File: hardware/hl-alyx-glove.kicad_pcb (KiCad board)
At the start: 2 copper layers, 2 parts, among them U1 MAX7219

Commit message: schematic first version
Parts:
- added D1: GREEN, LED_THT:LED_D5.0mm, F.Cu at (100.0, 49.0)
- added D2: GREEN, LED_THT:LED_D5.0mm, F.Cu at (95.0, 49.0)
- added D3: RED, LED_SMD:LED_2010_5025Metric, F.Cu at (169.0, 61.0)
- added J1: OLED, Connector_PinSocket_2.54mm:PinSocket_1x04_P2.54mm_Horizontal, B.Cu at (155.0, 97.0)
- added LED2: 788BS, CustomComponents:788BS, F.Cu at (123.5, 74.2)
- added LED3: 788BS, CustomComponents:788BS, F.Cu at (146.8, 74.6)
- added R1: 10K, Resistor_THT:R_Axial_DIN0309_L9.0mm_D3.2mm_P12.70mm_Horizontal, F.Cu at (106.0, 88.0)
- added R2: 10K, Resistor_THT:R_Axial_DIN0309_L9.0mm_D3.2mm_P12.70mm_Horizontal, F.Cu at (129.0, 88.0)
- added R3: 10K, Resistor_THT:R_Axial_DIN0309_L9.0mm_D3.2mm_P12.70mm_Horizontal, F.Cu at (152.0, 88.0)
- added R4: 10K, Resistor_THT:R_Axial_DIN0309_L9.0mm_D3.2mm_P12.70mm_Horizontal, F.Cu at (137.0, 49.0)
- added R5: 68, Resistor_THT:R_Axial_DIN0309_L9.0mm_D3.2mm_P12.70mm_Horizontal, F.Cu at (107.0, 57.0)
- added R6: 68, Resistor_THT:R_Axial_DIN0309_L9.0mm_D3.2mm_P12.70mm_Horizontal, F.Cu at (91.0, 60.0)
- added R7: 100, Resistor_THT:R_Axial_DIN0309_L9.0mm_D3.2mm_P12.70mm_Horizontal, F.Cu at (167.0, 49.0)
- added U2: MAX7219, Package_SO:SOP-24_7.5x15.4mm_P1.27mm, B.Cu at (123.5, 74.9)
- added U3: MAX7219, Package_SO:SOP-24_7.5x15.4mm_P1.27mm, B.Cu at (147.0, 74.6)
- added U4: ATmega328P-PU, Package_DIP:DIP-28_W7.62mm, F.Cu at (156.0, 53.0)
- U1: moved to B.Cu
- moved LED1 44.8 mm to (100.5, 73.8)
- moved U1 44.7 mm to (100.5, 73.8)
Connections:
- net Net-(U1-Pad4) renamed GND
- LED1 pad 1: Net-(LED1-Pad1) -> /LED_Matrix_0/C4
- LED1 pad 10: Net-(LED1-Pad10) -> /LED_Matrix_0/R4
- LED1 pad 11: Net-(LED1-Pad11) -> /LED_Matrix_0/R6
- LED1 pad 12: Net-(LED1-Pad12) -> /LED_Matrix_0/C5
- LED1 pad 13: Net-(LED1-Pad13) -> /LED_Matrix_0/R1
- LED1 pad 14: Net-(LED1-Pad14) -> /LED_Matrix_0/C7
- LED1 pad 15: Net-(LED1-Pad15) -> /LED_Matrix_0/R7
- LED1 pad 16: Net-(LED1-Pad16) -> /LED_Matrix_0/R8
- LED1 pad 2: Net-(LED1-Pad2) -> /LED_Matrix_0/C2
- LED1 pad 3: Net-(LED1-Pad3) -> /LED_Matrix_0/R2
- LED1 pad 4: Net-(LED1-Pad4) -> /LED_Matrix_0/R3
- LED1 pad 5: Net-(LED1-Pad5) -> /LED_Matrix_0/C1
- LED1 pad 6: Net-(LED1-Pad6) -> /LED_Matrix_0/R5
- LED1 pad 7: Net-(LED1-Pad7) -> /LED_Matrix_0/C3
- LED1 pad 8: Net-(LED1-Pad8) -> /LED_Matrix_0/C6
- LED1 pad 9: Net-(LED1-Pad9) -> /LED_Matrix_0/C8
- U1 pad 1: Net-(U1-Pad1) -> /LED_Matrix_0/DIN
- U1 pad 10: Net-(U1-Pad10) -> /LED_Matrix_0/R6
- U1 pad 11: Net-(U1-Pad11) -> /LED_Matrix_0/R2
- U1 pad 12: Net-(U1-Pad12) -> /LED_Matrix_0/LOAD
- U1 pad 13: Net-(U1-Pad13) -> /LED_Matrix_0/CLK
- U1 pad 14: Net-(U1-Pad14) -> /LED_Matrix_0/C2
- U1 pad 15: Net-(U1-Pad15) -> /LED_Matrix_0/C7
- U1 pad 16: Net-(U1-Pad16) -> /LED_Matrix_0/C3
- U1 pad 17: Net-(U1-Pad17) -> /LED_Matrix_0/C8
- U1 pad 2: Net-(U1-Pad2) -> /LED_Matrix_0/R1
- U1 pad 20: Net-(U1-Pad20) -> /LED_Matrix_0/C4
- U1 pad 21: Net-(LED1-Pad2) -> /LED_Matrix_0/C6
- U1 pad 22: Net-(U1-Pad22) -> /LED_Matrix_0/C1
- U1 pad 23: Net-(U1-Pad23) -> /LED_Matrix_0/C5
- U1 pad 24: Net-(U1-Pad24) -> /LED_Matrix_1/DIN
- U1 pad 3: Net-(U1-Pad3) -> /LED_Matrix_0/R5
- U1 pad 5: Net-(U1-Pad5) -> /LED_Matrix_0/R7
- U1 pad 6: Net-(U1-Pad6) -> /LED_Matrix_0/R3
- U1 pad 7: Net-(U1-Pad7) -> /LED_Matrix_0/R4
- U1 pad 8: Net-(U1-Pad8) -> /LED_Matrix_0/R8
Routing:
- net /LED_Matrix_1/R7: track 0.00 -> 26.6 mm, vias 0 -> 3
- net /LED_Matrix_2/R6: track 0.00 -> 22.5 mm, vias 0 -> 1
- net /LED_Matrix_1/R6: track 0.00 -> 22.5 mm, vias 0 -> 1
- net /LED_Matrix_0/R6: track 0.00 -> 22.5 mm, vias 0 -> 1
- net GND: track 0.00 -> 21.0 mm, vias 0 -> 4
- net /LED_Matrix_2/C3: track 0.00 -> 19.2 mm, vias 0 -> 3
- net /LED_Matrix_1/C3: track 0.00 -> 19.2 mm, vias 0 -> 3
- net /LED_Matrix_0/C3: track 0.00 -> 19.2 mm, vias 0 -> 3
- net /LED_Matrix_2/C4: track 0.00 -> 18.7 mm
- net /LED_Matrix_1/C4: track 0.00 -> 18.7 mm
- net /LED_Matrix_0/C4: track 0.00 -> 18.7 mm
- net /LED_Matrix_1/R4: track 0.00 -> 17.9 mm, vias 0 -> 1
- net /LED_Matrix_0/R4: track 0.00 -> 17.9 mm, vias 0 -> 1
- net /LED_Matrix_2/R4: track 0.00 -> 17.9 mm, vias 0 -> 1
- net /LED_Matrix_2/R1: track 0.00 -> 16.7 mm, vias 0 -> 1
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
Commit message: add some missing components
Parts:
- added C1: 100N, Capacitor_THT:C_Disc_D6.0mm_W2.5mm_P5.00mm, F.Cu at (126.0, 49.0)
- added J2: POWER, Connector_PinHeader_2.54mm:PinHeader_1x02_P2.54mm_Horizontal, F.Cu at (112.0, 44.0)
- moved U2 0.69 mm to (123.5, 74.2)
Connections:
- U1 pad 19: Net-(U1-Pad19) -> +3V3
- U2 pad 19: Net-(U2-Pad19) -> +3V3
- U3 pad 19: Net-(U3-Pad19) -> +3V3
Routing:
- net GND: track 21.0 -> 31.6 mm, vias 4 -> 6
- net /LED_Matrix_1/R7: track 26.6 -> 16.1 mm, vias 3 -> 1

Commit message: pcb first version
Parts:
- added REF**: MountingHole_3.2mm_M3, MountingHole:MountingHole_3.2mm_M3, F.Cu at (88.0, 90.0)
- added REF**: MountingHole_3.2mm_M3, MountingHole:MountingHole_3.2mm_M3, F.Cu at (88.0, 54.0)
- added REF**: MountingHole_3.2mm_M3, MountingHole:MountingHole_3.2mm_M3, F.Cu at (170.0, 48.0)
- added REF**: MountingHole_3.2mm_M3, MountingHole:MountingHole_3.2mm_M3, F.Cu at (145.0, 90.0)
- D3: footprint LED_SMD:LED_2010_5025Metric -> LED_SMD:LED_RGB_5050-6
- J2: moved to B.Cu
- R7: value 100 -> 180
- moved J2 36.8 mm to (87.0, 71.0), turned to 180 degrees
- moved R4 34.1 mm to (171.0, 51.5), turned to 180 degrees
- moved J1 21.5 mm to (164.0, 77.5)
- moved C1 16.3 mm to (137.5, 60.5)
- moved R3 13.5 mm to (138.5, 88.0)
- moved D3 10.7 mm to (163.2, 70.0), turned to 0 degrees
- moved D1 10.1 mm to (110.0, 47.5), turned to 270 degrees
- moved R7 8.50 mm to (171.0, 56.5)
- moved R2 7.00 mm to (122.0, 88.0)
- moved D2 5.22 mm to (100.0, 47.5), turned to 270 degrees
- moved U3 4.90 mm to (142.1, 74.6)
- moved LED3 4.90 mm to (141.9, 74.6)
- moved R6 4.12 mm to (95.0, 59.0)
- moved U4 3.64 mm to (155.0, 49.5)
- moved U2 2.82 mm to (120.7, 74.6)
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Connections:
- D3 pad 2: Net-(D3-Pad2) -> GND
- J2 pad 1: +3V3 -> GND
- J2 pad 2: GND -> +3V3
- R7 pad 1: Net-(D3-Pad2) -> Net-(D3-Pad4)
- U4 pad 11: Net-(R6-Pad2) -> Net-(U4-Pad11)
- U4 pad 12: Net-(R5-Pad2) -> Net-(U4-Pad12)
- U4 pad 13: Net-(R7-Pad2) -> Net-(R5-Pad2)
- U4 pad 14: Net-(U4-Pad14) -> Net-(R6-Pad2)
- U4 pad 15: Net-(U4-Pad15) -> /LED_Matrix_0/DIN
- U4 pad 18: /LED_Matrix_0/DIN -> Net-(U4-Pad18)
- U4 pad 3: Net-(U4-Pad3) -> Net-(R7-Pad2)
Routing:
- net +3V3: track 0.00 -> 246.7 mm, vias 0 -> 3
- net /LED_Matrix_0/LOAD: track 0.00 -> 74.6 mm, vias 0 -> 3
- net /LED_Matrix_0/CLK: track 0.00 -> 64.2 mm
- net /LED_Matrix_0/DIN: track 0.00 -> 57.9 mm
- net Net-(J1-Pad1): track 0.00 -> 25.5 mm
- net Net-(J1-Pad2): track 0.00 -> 23.1 mm
- net Net-(D3-Pad4): track 0.00 -> 18.6 mm
- net Net-(R6-Pad2): track 0.00 -> 18.2 mm
- net /LED_Matrix_1/DIN: track 0.00 -> 17.8 mm
- net /LED_Matrix_2/DIN: track 0.00 -> 17.8 mm
- net Net-(R7-Pad2): track 0.00 -> 11.3 mm
- net Net-(D2-Pad2): track 0.00 -> 11.0 mm
- net Net-(R1-Pad1): track 7.11 -> 17.9 mm
- net GND: track 31.6 -> 40.7 mm
- net Net-(R5-Pad2): track 0.00 -> 8.10 mm
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- added copper zone on B.Cu, net GND
- added copper zone on F.Cu, net GND
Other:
- board outline added: 88 x 48 mm
- board text added: "CHRZ 2021"

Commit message: Add rev 1 gerber files
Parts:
- moved R4 1.00 mm to (171.0, 52.5)
- moved J2 0.60 mm to (87.6, 71.0)
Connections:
- U4 pad 3: Net-(R7-Pad2) -> Net-(U4-Pad3)
- U4 pad 4: Net-(U4-Pad4) -> Net-(R7-Pad2)
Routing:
- net Net-(R7-Pad2): track 11.3 -> 13.8 mm
- net /LED_Matrix_0/C6: track 15.8 -> 15.1 mm
- net GND: track 40.7 -> 40.1 mm
- net /LED_Matrix_2/C3: track 19.2 -> 18.6 mm
- net /LED_Matrix_0/C3: track 19.2 -> 18.7 mm
- net /LED_Matrix_1/C3: track 19.2 -> 18.7 mm
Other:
- board text added: "HL:A G R1 CHRZ 2021"
- board text removed: "CHRZ 2021"

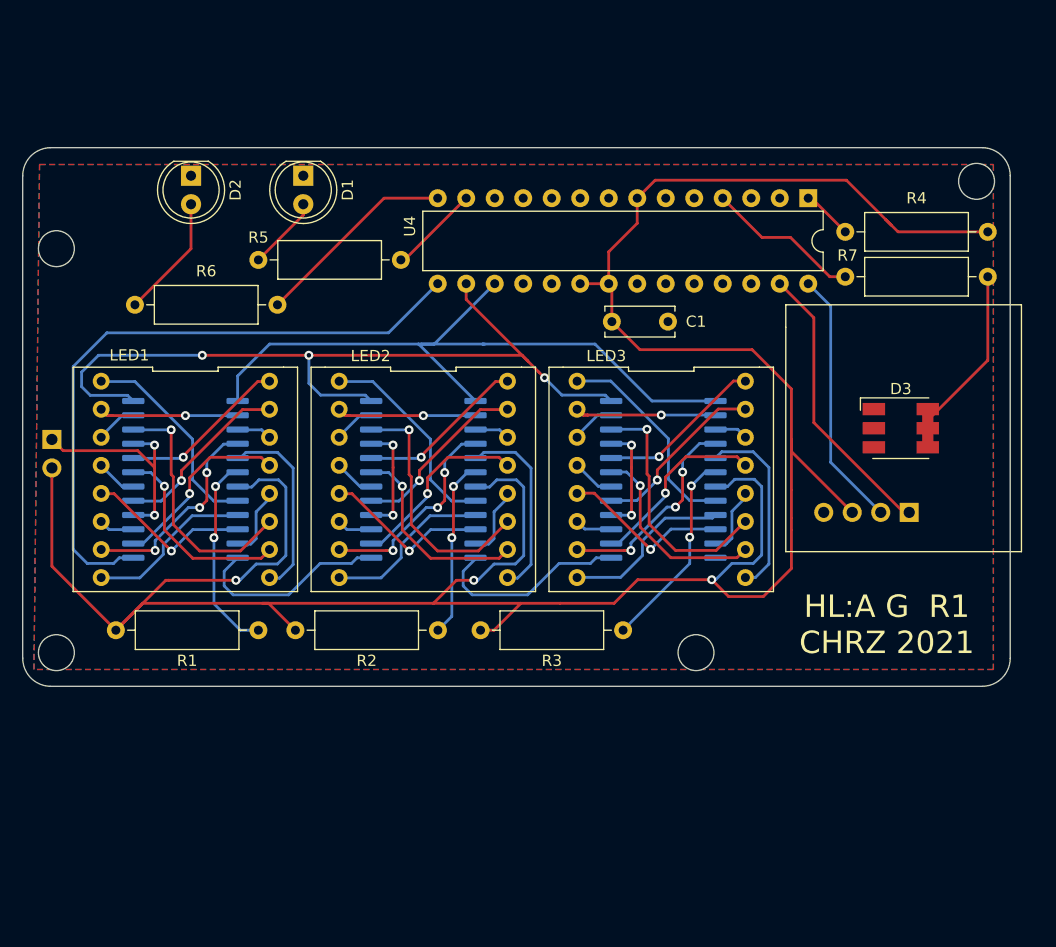
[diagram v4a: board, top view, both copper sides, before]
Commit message: PCB rev 2 first changes
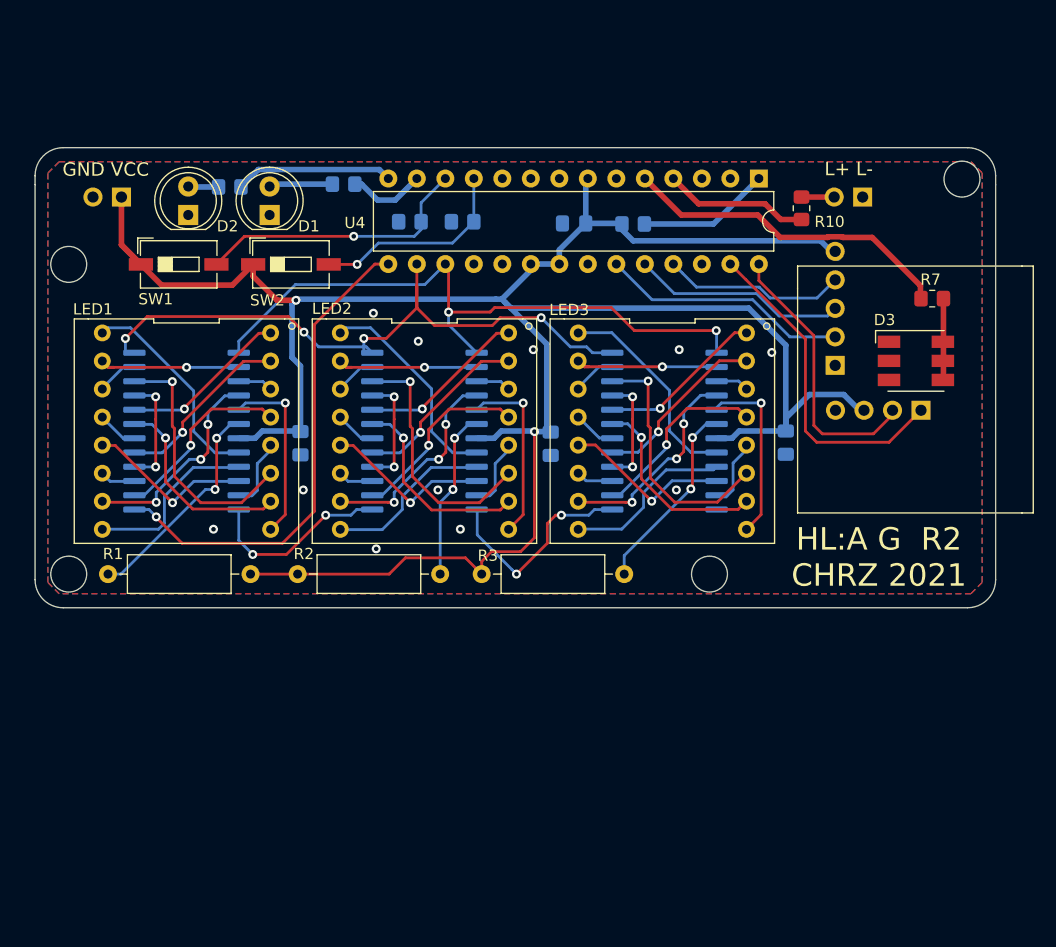
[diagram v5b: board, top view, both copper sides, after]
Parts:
- removed J1: OLED, Connector_PinSocket_2.54mm:PinSocket_1x04_P2.54mm_Horizontal
- removed J2: POWER, Connector_PinHeader_2.54mm:PinHeader_1x02_P2.54mm_Horizontal
- removed the REF** at (88.0, 90.0)
- removed the REF** at (88.0, 54.0)
- removed the REF** at (170.0, 48.0)
- removed the REF** at (145.0, 90.0)
- added ACCEL: IMU, Connector_PinSocket_2.54mm:PinSocket_1x05_P2.54mm_Vertical, B.Cu at (157.4, 64.4)
- added C2: 100N, Capacitor_SMD:C_0805_2012Metric_Pad1.18x1.45mm_HandSolder, B.Cu at (109.8, 71.3)
- added C3: 100N, Capacitor_SMD:C_0805_2012Metric_Pad1.18x1.45mm_HandSolder, B.Cu at (132.1, 71.4)
- added C4: 100N, Capacitor_SMD:C_0805_2012Metric_Pad1.18x1.45mm_HandSolder, B.Cu at (153.0, 71.3)
- added DISPLAY: OLED, Connector_PinSocket_2.54mm:PinSocket_1x04_P2.54mm_Horizontal, B.Cu at (165.1, 68.4)
- added H1: MountingHole, MountingHole:MountingHole_3.2mm_M3_DIN965, F.Cu at (168.7, 47.8)
- added H2: MountingHole, MountingHole:MountingHole_3.2mm_M3_DIN965, F.Cu at (89.1, 55.4)
- added H3: MountingHole, MountingHole:MountingHole_3.2mm_M3_DIN965, F.Cu at (146.2, 83.0)
- added H4: MountingHole, MountingHole:MountingHole_3.2mm_M3_DIN965, F.Cu at (89.1, 83.0)
- added LED: EXT_LED, Connector_PinHeader_2.54mm:PinHeader_1x02_P2.54mm_Horizontal, B.Cu at (159.8, 49.4)
- added POWER: POWER, Connector_PinHeader_2.54mm:PinHeader_1x02_P2.54mm_Horizontal, B.Cu at (93.8, 49.4)
- added R10: 180, Resistor_SMD:R_0805_2012Metric_Pad1.20x1.40mm_HandSolder, F.Cu at (154.4, 50.4)
- added R8: 10K, Resistor_SMD:R_0805_2012Metric_Pad1.20x1.40mm_HandSolder, B.Cu at (124.2, 51.6)
- added R9: 10K, Resistor_SMD:R_0805_2012Metric_Pad1.20x1.40mm_HandSolder, B.Cu at (119.5, 51.6)
- added REF**: OSHW-Logo2_7.3x6mm_SilkScreen, Symbol:OSHW-Logo2_7.3x6mm_SilkScreen, B.Cu at (99.3, 56.2)
- added SW1: SW_Push, Button_Switch_SMD:SW_DIP_SPSTx01_Slide_6.7x4.1mm_W6.73mm_P2.54mm_LowProfile_JPin, F.Cu at (98.9, 55.4)
- added SW2: SW_Push, Button_Switch_SMD:SW_DIP_SPSTx01_Slide_6.7x4.1mm_W6.73mm_P2.54mm_LowProfile_JPin, F.Cu at (108.9, 55.4)
- C1: footprint Capacitor_THT:C_Disc_D6.0mm_W2.5mm_P5.00mm -> Capacitor_SMD:C_0805_2012Metric_Pad1.18x1.45mm_HandSolder; moved to B.Cu
- R4: footprint Resistor_THT:R_Axial_DIN0309_L9.0mm_D3.2mm_P12.70mm_Horizontal -> Resistor_SMD:R_0805_2012Metric_Pad1.20x1.40mm_HandSolder; moved to B.Cu
- R5, R6: value 68 -> 180; footprint Resistor_THT:R_Axial_DIN0309_L9.0mm_D3.2mm_P12.70mm_Horizontal -> Resistor_SMD:R_0805_2012Metric_Pad1.20x1.40mm_HandSolder; moved to B.Cu
- R7: footprint Resistor_THT:R_Axial_DIN0309_L9.0mm_D3.2mm_P12.70mm_Horizontal -> Resistor_SMD:R_0805_2012Metric_Pad1.20x1.40mm_HandSolder
- moved R4 31.6 mm to (139.4, 51.8), turned to 0 degrees
- moved R1 14.3 mm to (92.6, 83.0), turned to 0 degrees
- moved R6 13.5 mm to (103.5, 48.5)
- moved R5 10.2 mm to (113.6, 48.2)
- moved C1 9.37 mm to (134.1, 51.8), turned to 180 degrees
- moved D3 6.15 mm to (164.6, 64.0)
- moved R7 5.32 mm to (166.1, 58.5)
- moved R2 5.00 mm to (122.2, 83.0)
- moved R3 5.00 mm to (138.6, 83.0)
- moved U4 4.74 mm to (150.6, 47.8)
- moved D1 4.61 mm to (107.0, 51.0), turned to 90 degrees
- moved LED1 4.30 mm to (99.6, 70.3)
- moved LED2 4.30 mm to (120.8, 70.3)
- moved LED3 4.30 mm to (142.0, 70.3)
- moved U1 4.30 mm to (99.6, 70.3)
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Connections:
- net +3V3 renamed VCC
- U4 pad 4: Net-(R7-Pad2) -> Net-(R10-Pad2)
- U4 pad 5: Net-(U4-Pad5) -> Net-(R7-Pad2)
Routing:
- net VCC: track 246.2 -> 212.8 mm, vias 3 -> 2
- net Net-(R9-Pad2): track 0.00 -> 25.0 mm, vias 0 -> 1
- net Net-(J3-Pad2): track 0.00 -> 22.2 mm
- net Net-(J3-Pad3): track 0.00 -> 19.2 mm
- net Net-(R8-Pad2): track 0.00 -> 18.4 mm, vias 0 -> 1
- net Net-(J3-Pad4): track 0.00 -> 16.3 mm
- net Net-(R7-Pad2): track 13.8 -> 29.7 mm
- net /LED_Matrix_0/LOAD: track 74.6 -> 59.8 mm, vias 3 -> 4
- net /LED_Matrix_0/DIN: track 57.9 -> 44.0 mm, vias 0 -> 1
- net Net-(R10-Pad2): track 0.00 -> 12.9 mm
- net Net-(D3-Pad4): track 18.6 -> 7.48 mm
- net GND: track 40.1 -> 29.9 mm, vias 6 -> 17
- net Net-(D2-Pad2): track 11.0 -> 2.72 mm
- net Net-(R4-Pad2): track 4.54 -> 12.2 mm
- net /LED_Matrix_0/CLK: track 64.2 -> 58.2 mm, vias 0 -> 2
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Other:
- board size 88 x 48 mm -> 85.6 x 41 mm
- rule trace_min: 0.2 -> 0.127
- rule via_min_size: 0.4 -> 0.2
- board text added: "C"
- board text added: "D"
- board text added: "G"
- board text added: "GND VCC"
- board text added: "GitHub.com/ StarGate01/ hl-alyx-glove"
- board text added: "HL:A G R2 CHRZ 2021"
- board text added: "L+ L-"
- board text added: "V"
- board text added: "X"
- board text added: "Y"
- board text added: "Z"
- board text removed: "HL:A G R1 CHRZ 2021"

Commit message: add second led
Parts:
- removed the LED at (159.8, 49.4)
- added LED: EXT_LED, Connector_PinHeader_2.54mm:PinHeader_1x03_P2.54mm_Horizontal, B.Cu at (162.1, 49.4)
- added R11: 180, Resistor_SMD:R_0805_2012Metric_Pad1.20x1.40mm_HandSolder, F.Cu at (158.6, 51.5)
- moved REF** 0.36 mm to (99.7, 56.3)
- renumbered ACCEL to SENSOR
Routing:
- net Net-(R10-Pad2): track 12.9 -> 16.1 mm
- net Net-(J4-Pad2): track 0.00 -> 2.15 mm
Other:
- board text added: "G 5V"
- board text added: "L1"
- board text added: "L2"
- board text removed: "GND VCC"
- board text removed: "L+ L-"

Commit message: add missing resistors to big led
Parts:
- added R12: 180, Resistor_SMD:R_0805_2012Metric_Pad1.20x1.40mm_HandSolder, F.Cu at (165.3, 58.4)
- added R13: 180, Resistor_SMD:R_0805_2012Metric_Pad1.20x1.40mm_HandSolder, F.Cu at (162.7, 58.4)
- moved R7 1.70 mm to (167.8, 58.4), turned to 90 degrees
- renumbered DISPLAY to J1, POWER to J2, SENSOR to J3, LED to J4
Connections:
- D3 pad 5: Net-(D3-Pad4) -> Net-(D3-Pad5)
- D3 pad 6: Net-(D3-Pad4) -> Net-(D3-Pad6)
- R7 pad 1: Net-(D3-Pad4) -> Net-(D3-Pad6)
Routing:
- net Net-(D3-Pad5): track 0.00 -> 6.21 mm
- net Net-(D3-Pad6): track 0.00 -> 3.21 mm
- net Net-(D3-Pad4): track 7.48 -> 9.18 mm
- net Net-(R12-Pad2): track 29.7 -> 31.3 mm

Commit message: small fixes
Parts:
- moved C3 0.15 mm to (132.2, 71.4)
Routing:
- net VCC: track 212.8 -> 211.0 mm
- net Net-(R1-Pad1): track 19.8 -> 20.6 mm
- net /LED_Matrix_2/C8: track 16.2 -> 17.0 mm
- net /LED_Matrix_0/C8: track 16.6 -> 17.3 mm
- net GND: vias 17 -> 18
